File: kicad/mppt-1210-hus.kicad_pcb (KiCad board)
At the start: 2 copper layers, 90 x 85 mm, 136 parts, among them J1 MKDS_5-2_952, J2 MKDS_5-2_952, J3 MKDS_5-2_952, J4 UEXT, J5 USB_A_stacked, J6 PWR_12V, J7 6P6C, J8 ST_Nucleo_SWD, Q1 PSMN5R2-60YLX, Q2 PSMN5R2-60YLX, Q3 BSC084P03NS3, Q4 PSMN5R2-60YLX, Q5 BSS83P, Q6 BSS83P, Q7 BSS83P, T1 MMBT3904, T2 MMBT3904, U1 LM5109BMA, U2 STM32L072CZT6, U3 D1213A-04SO, U4 D1213A-04SO, U5 AP2210-3.3, U6 INA2181, U9 LMR33630

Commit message: Small changes and files renamed
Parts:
- R32: value 1M -> 100k
- R36: value 10k -> 100k
- moved R7 23.5 mm to (173.7, 84.6), turned to 0 degrees
- moved REF** 15.5 mm to (98.1, 65.0)
- moved REF** 11.4 mm to (174.5, 127.0)
- moved J8 9.21 mm to (107.3, 58.5), turned to 90 degrees
- moved LED1 2.12 mm to (180.8, 79.0), turned to 90 degrees
- moved LED2 2.12 mm to (180.8, 86.0), turned to 90 degrees
- moved LED3 2.12 mm to (180.8, 93.0), turned to 90 degrees
- moved LED4 2.12 mm to (180.8, 105.0), turned to 90 degrees
- moved LED5 2.12 mm to (180.8, 67.0), turned to 90 degrees
- moved LOGO1 0.80 mm to (171.4, 90.7)
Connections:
- C43 pad 1: /MCU/BUTTON -> /MCU/BOOT0
- R33 pad 2: /MCU/BUTTON -> /MCU/BOOT0
- R35 pad 1: +3V3 -> GND
- R35 pad 2: /MCU/BUTTON -> /MCU/BOOT0
- R7 pad 1: /MCU/BOOT0 -> /MCU/BUTTON
- R7 pad 2: GND -> /MCU/BOOT0
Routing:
- net /MCU/BOOT0: track 8.36 -> 66.6 mm, vias 2 -> 4
- net /MCU/BUTTON: track 54.3 -> 8.21 mm, vias 2 -> 0
- net /MCU/~RESET: track 63.4 -> 52.3 mm, vias 4 -> 5
- net +3V3: track 188.8 -> 197.9 mm
- net /MCU/SWDIO: track 89.0 -> 83.3 mm, vias 1 -> 2
- net /MCU/SWCLK: track 75.1 -> 80.5 mm
- net Net-(LED1-Pad2): track 22.1 -> 25.8 mm
- net /MCU/LED_B: track 36.3 -> 38.8 mm
- net GND: track 59.4 -> 57.2 mm, vias 75 -> 72
- net Net-(LED4-Pad1): track 49.1 -> 48.0 mm
- net /MCU/LED_C: track 65.6 -> 66.3 mm, vias 2 -> 1
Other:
- board text added: "Design: Martin Jäger | https://libre.solar | 06/2019"
- board text added: "MPPT charge controller evaluation board for custom developments. Warning: Do not use in end-user products!"
- board text added: "MPPT-1210-HUS"
- board text added: "v0.7"
- board text removed: "10A MPPT Charger"
- board text removed: "Design: Martin Jäger | https://libre.solar"
- board text removed: "V0.6 (04/2019)"

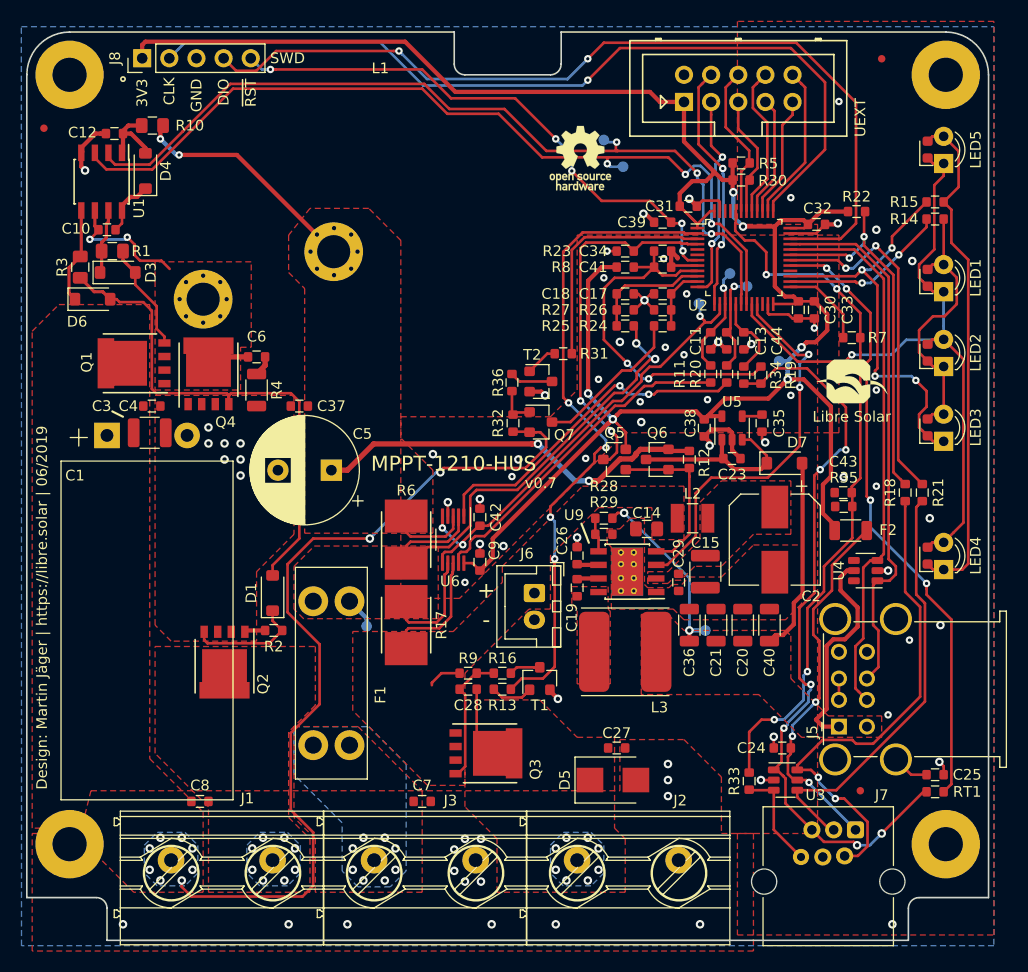
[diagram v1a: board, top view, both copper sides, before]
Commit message: Small adjustments after testing
- MOSFET gate driver changed to reduce switch node ringing
- Current measurement output filter time constant reduced to have less delay
- BTN pin allows starting the bootloader if pulled to 3V3 before startup
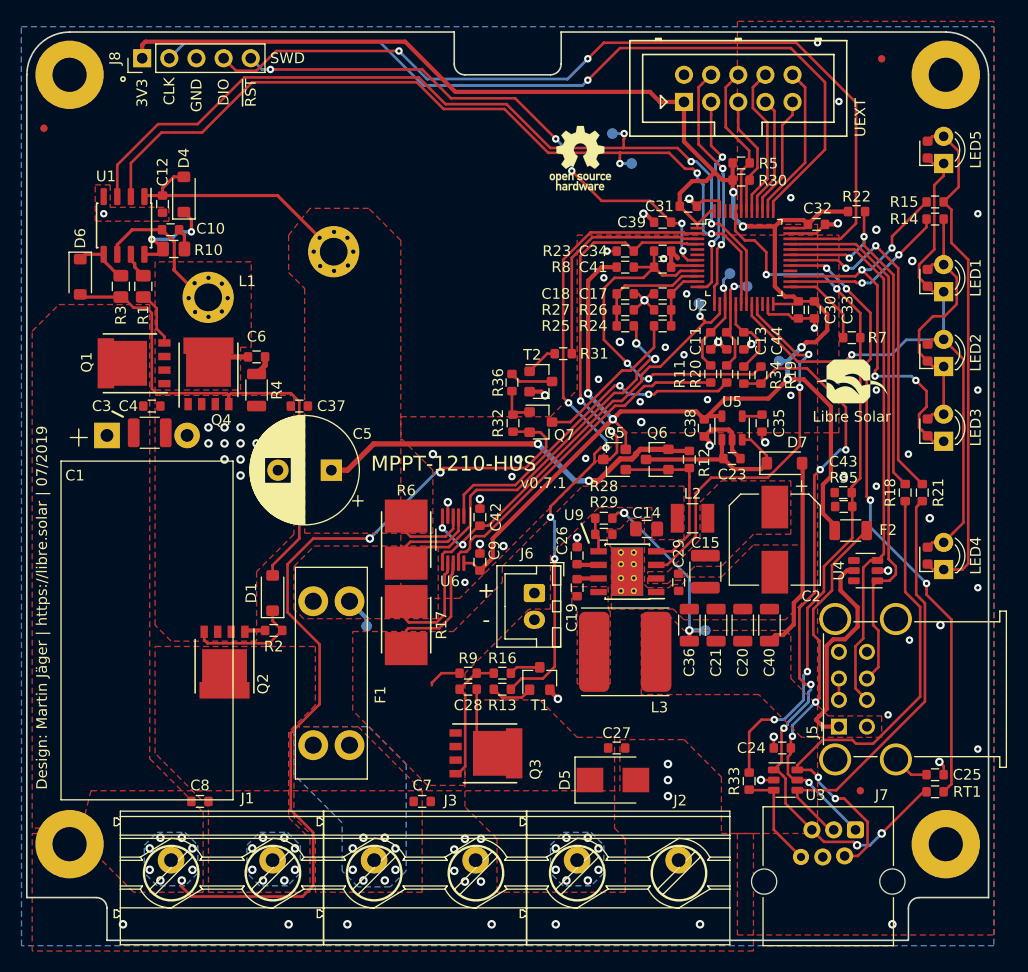
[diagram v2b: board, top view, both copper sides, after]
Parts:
- removed D3: SS14FL, LibreSolar:D_SOD-123
- C11, C13: value 10n -> 1n
- L1: footprint LibreSolar:L-FERYSTER-DTMSS-27_33uH -> LibreSolar:L-FERYSTER-DTMSS-27_47uH
- R11, R20: value 2.2k -> 470
- R32: value 100k -> 24.9k
- U1: footprint Package_SO:SOIC-8_3.9x4.9mm_P1.27mm -> LibreSolar:SOIC-8_3.9x4.9mm_Pitch1.27mm
- moved R10 11.7 mm to (110.2, 76.3), turned to 180 degrees
- moved C12 7.99 mm to (109.2, 72.1), turned to 270 degrees
- moved C10 5.95 mm to (110.0, 74.5)
- moved U1 4.61 mm to (105.6, 74.1)
- moved R1 4.39 mm to (107.4, 79.8), turned to 90 degrees
- moved D4 4.22 mm to (111.2, 71.2)
- moved R3 4.20 mm to (105.3, 79.8)
- moved TP2 3.41 mm to (153.1, 68.3)
- moved TP3 3.26 mm to (151.3, 65.5)
- moved D6 2.39 mm to (101.5, 78.9), turned to 270 degrees
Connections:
- C12 pad 1: Net-(C12-Pad1) -> DCDC_OUT
- D4 pad 1: Net-(C10-Pad1) -> Net-(D4-Pad1)
- D4 pad 2: Net-(C12-Pad1) -> DCDC_OUT
- R10 pad 1: Net-(C12-Pad1) -> Net-(C10-Pad1)
- R10 pad 2: DCDC_OUT -> Net-(D4-Pad1)
- U1 pad 1: Net-(C12-Pad1) -> DCDC_OUT
- U1 pad 8: Net-(C10-Pad1) -> Net-(D4-Pad1)
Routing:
- net Net-(D4-Pad1): track 0.00 -> 9.50 mm, vias 0 -> 2
- net Net-(C12-Pad1): track 7.21 -> 0.00 mm
- net Net-(Q1-PadG): track 10.7 -> 5.23 mm
- net GND: track 57.2 -> 51.9 mm, vias 72 -> 83
- net /DCDC power stage/LS_DRV: track 9.00 -> 5.16 mm
- net /DCDC power stage/HS_DRV: track 6.13 -> 2.48 mm
- net Net-(C10-Pad1): track 5.37 -> 2.01 mm
- net /DCDC power stage/SW_NODE: track 16.7 -> 17.9 mm, vias 10 -> 8
- net DCDC_OUT: track 66.8 -> 67.9 mm, vias 12 -> 10
- net Net-(D1-Pad2): track 48.7 -> 47.9 mm
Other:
- rule solder_mask_min_width: 0.25 -> 0.2
- board text added: "Design: Martin Jäger | https://libre.solar | 07/2019"
- board text added: "v0.7.1"
- board text removed: "Design: Martin Jäger | https://libre.solar | 06/2019"
- board text removed: "v0.7"
